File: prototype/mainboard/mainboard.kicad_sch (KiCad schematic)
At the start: 24 parts, among them J1 measuring_input4, J11 STM32G474_MCU_right_header, J12 STM32G474_MCU_left_header, J17 usb_B, J2 measuring_input4, J3 measuring_input4, J4 measuring_input4, J5 measuring_input4

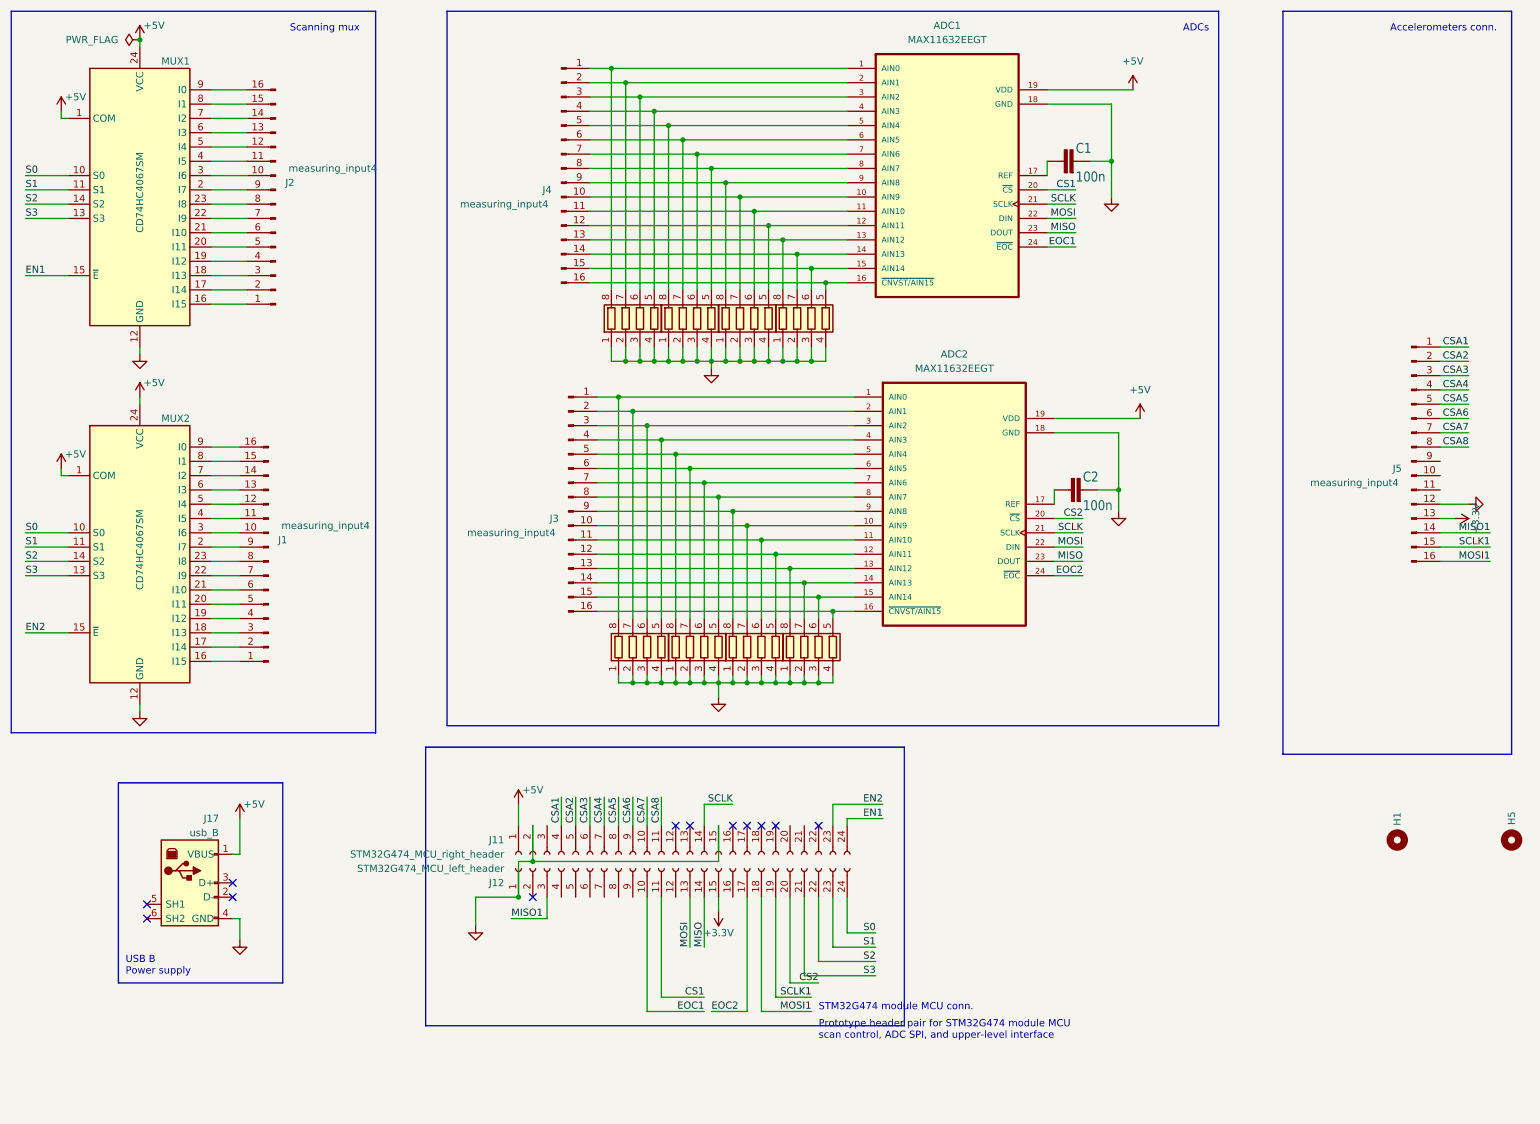
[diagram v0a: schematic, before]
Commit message: Connect STM32G474CETx in prototype schematic
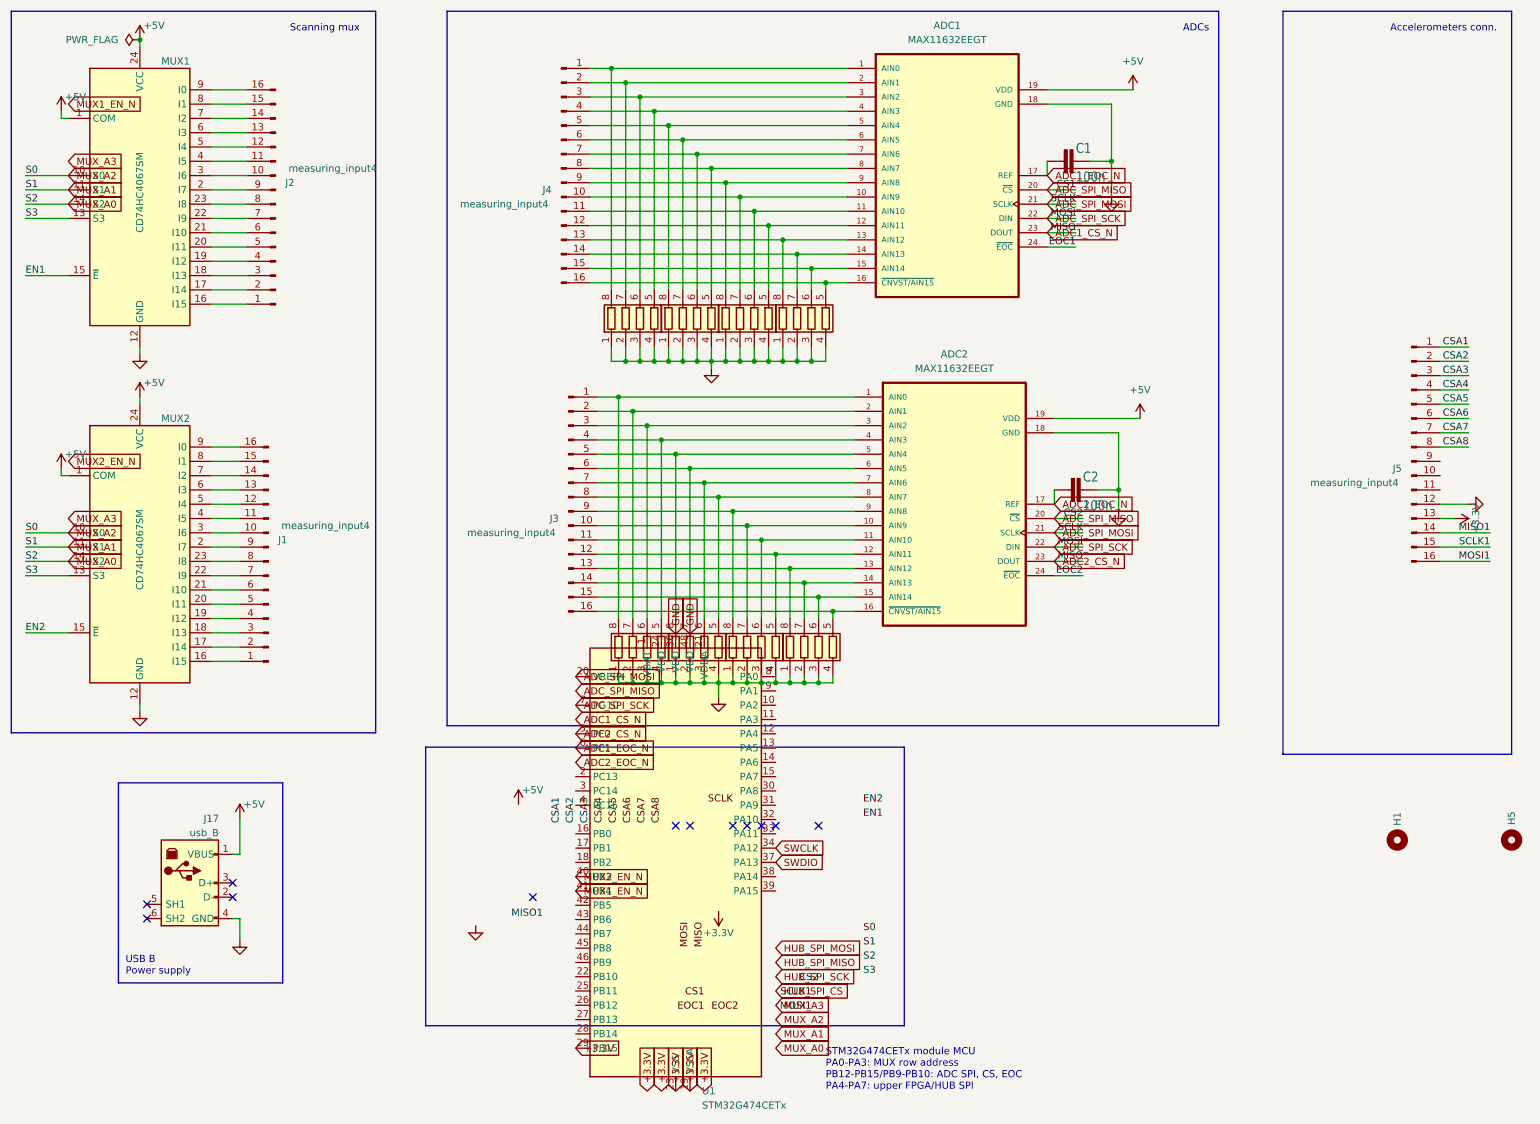
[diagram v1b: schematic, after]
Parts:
- removed J11: STM32G474_MCU_right_header, Connector_PinSocket_2.54mm:PinSocket_1x24_P2.54mm_Vertical, symbol Connector:Conn_01x24_Female
- removed J12: STM32G474_MCU_left_header, Connector_PinSocket_2.54mm:PinSocket_1x24_P2.54mm_Vertical, symbol Connector:Conn_01x24_Female
- added U1: STM32G474CETx, Package_QFP:LQFP-48_7x7mm_P0.5mm, symbol MCU_ST_STM32G4:STM32G474CETx
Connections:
- net CS2 is gone; now on net ADC_SPI_MISO: ADC2.20 (~{CS})
- net +3.3V: now also U1.19 (VSSA), U1.23 (VSS), U1.29 (PB15), U1.35 (VSS), U1.47 (VSS)
- net GND: now also U1.36 (VDD), U1.48 (VDD)
- net ADC1_EOC_N: now reaches ADC1.17 (REF), C1.1
- net ADC1_EOC_N: now also U1.6 (PF1)
- net ADC2_EOC_N: now reaches ADC2.17 (REF), C2.1
- net CS1 renamed ADC_SPI_MISO
- net MISO renamed ADC1_CS_N
- net ADC1_CS_N: now also U1.5 (PF0)
- net MOSI renamed ADC_SPI_SCK
- net ADC_SPI_SCK: now also U1.7 (PG10)
- net S0 renamed MUX_A2
- net S1 renamed MUX_A1
- net S2 renamed MUX_A0
- net SCLK renamed ADC_SPI_MOSI
- net ADC_SPI_MOSI: now also U1.20 (VREF+)
- new net MUX1_EN_N: U1.41 (PB4)
- new net MUX2_EN_N: U1.40 (PB3)
- new net SWCLK: U1.34 (PA12)
- new net SWDIO: U1.37 (PA13)
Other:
- note added: "STM32G474CETx module MCU PA0-PA3: MUX row address PB12-PB15/PB9-PB10: ADC SPI, CS, EOC PA4-PA7: upper FPGA/HUB SPI"
- note removed: "Prototype header pair for STM32G474 module MCU scan control, ADC SPI, and upper-level interface"
- note removed: "STM32G474 module MCU conn."
